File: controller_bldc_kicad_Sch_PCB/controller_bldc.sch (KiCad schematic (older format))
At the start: 57 parts, among them J1 Battery Supply, J2 Emergency Button OUT, J3 Emergency Button IN, J4 Brake, J5 Throttle, J6 LM35, J7 Hall Sensors, J8 Nextion Nx3224T028, J9 BLDC Motor, K1 ADW11, Q1 IRF1010N, Q2 IRF1010N, Q3 IRF1010N, Q4 IRF1010N, Q5 IRF1010N, Q6 IRF1010N, SW1 ON_OFF, SW2 OPC, U1 ESP32-DEVKITC-32D, U2 LM317_TO-220, U3 LM7805_TO220, U4 IR2103, U8 IR2103, U9 IR2103

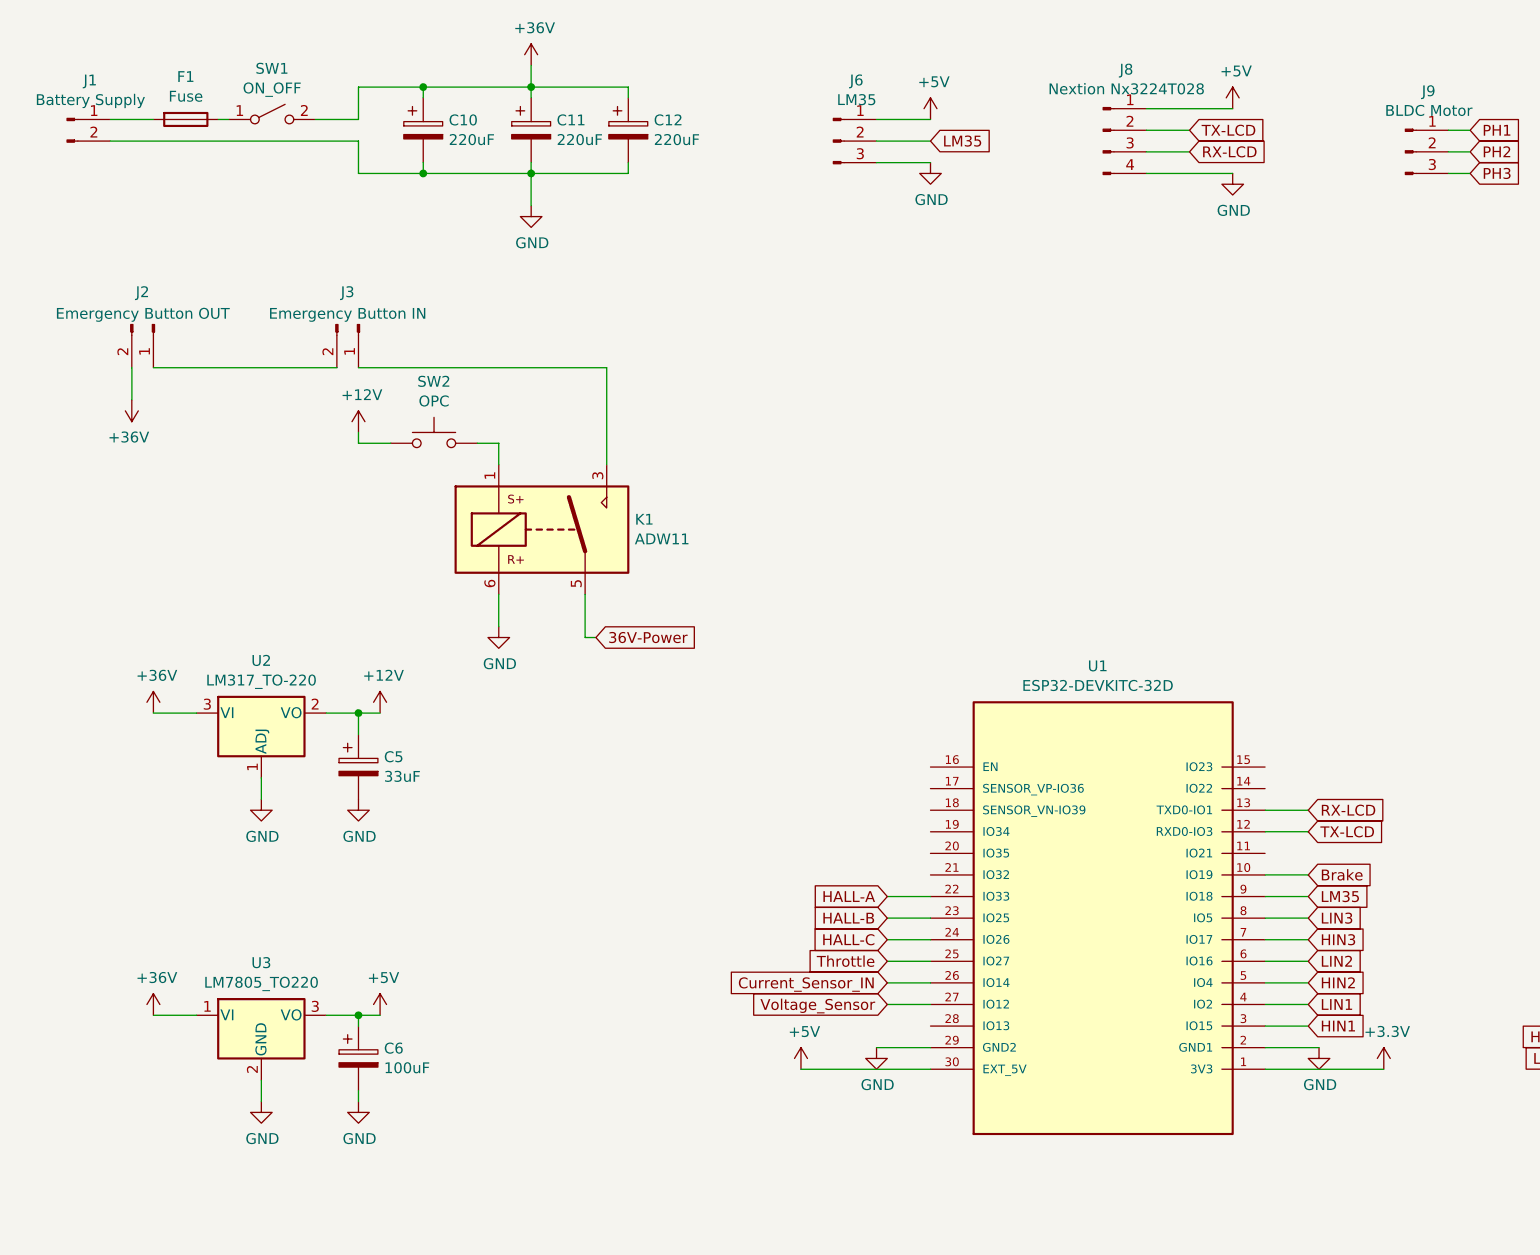
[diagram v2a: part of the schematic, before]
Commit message: Fixed the schematic for the three 220uF capacitors and the connections Connections of MCPWM GPIOs inside the main/*.c were changed to correspond with the schematic
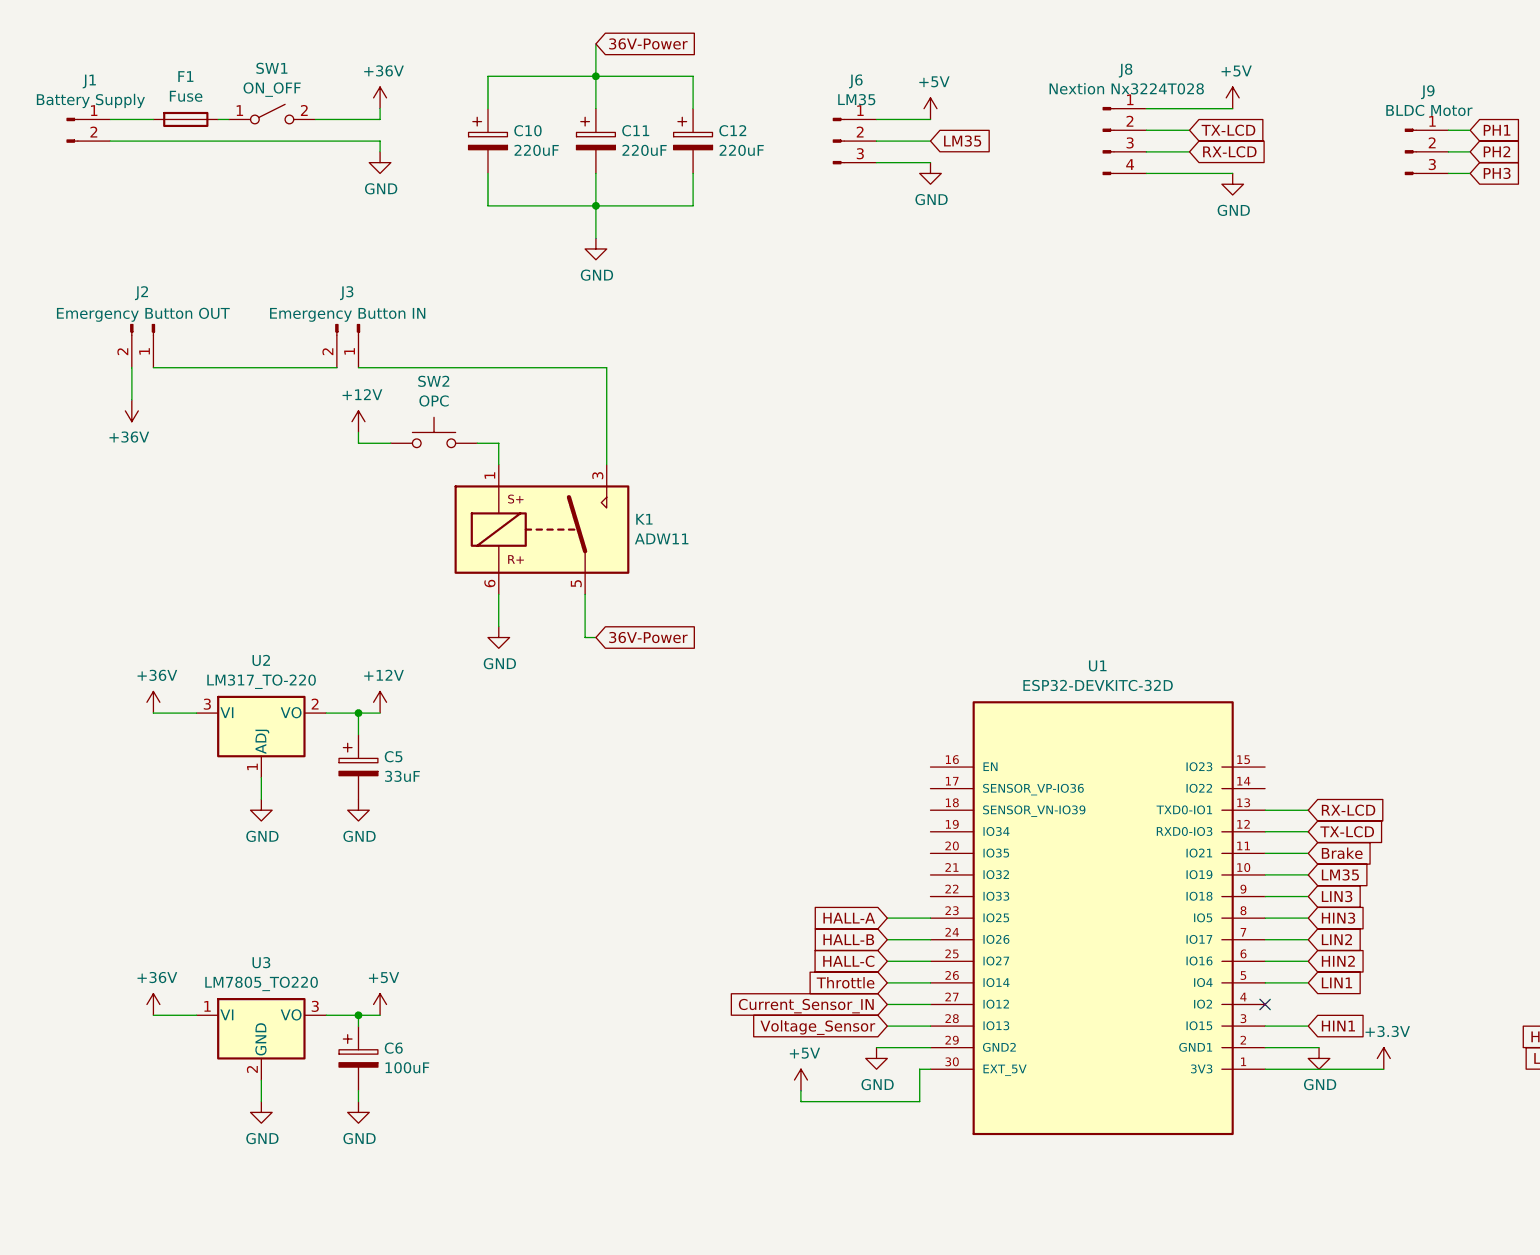
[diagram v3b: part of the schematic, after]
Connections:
- net +36V: no longer C10.1, C11.1, C12.1
- net 36V-Power: now also C10.1, C11.1, C12.1
- net Brake: now also U1.11 (IO21); no longer U1.10 (IO19)
- net Current_Sensor_IN: now also U1.27 (IO12); no longer U1.26 (IO14)
- net HALL-A: now also U1.23 (IO25); no longer U1.22 (IO33)
- net HALL-B: now also U1.24 (IO26); no longer U1.23 (IO25)
- net HALL-C: now also U1.25 (IO27); no longer U1.24 (IO26)
- net HIN2: now also U1.6 (IO16); no longer U1.5 (IO4)
- net HIN3: now also U1.8 (IO5); no longer U1.7 (IO17)
- net LIN1: now also U1.5 (IO4); no longer U1.4 (IO2)
- net LIN2: now also U1.7 (IO17); no longer U1.6 (IO16)
- net LIN3: now also U1.9 (IO18); no longer U1.8 (IO5)
- net LM35: now also U1.10 (IO19); no longer U1.9 (IO18)
- net Throttle: now also U1.26 (IO14); no longer U1.25 (IO27)
- net Voltage_Sensor: now also U1.28 (IO13); no longer U1.27 (IO12)
- no-connect marks 0 -> 1
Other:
- moved on the sheet: C10, C11, C12
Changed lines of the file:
@@
 L power:GND #PWR08
 U 1 1 6069EAE5
-P 2500 900
-F 0 "#PWR08" H 2500 650 50  0001 C CNN
-F 1 "GND" H 2505 727 50  0000 C CNN
-F 2 "" H 2500 900 50  0001 C CNN
-F 3 "" H 2500 900 50  0001 C CNN
-	1    2500 900
+P 1800 650
+F 0 "#PWR08" H 1800 400 50  0001 C CNN
+F 1 "GND" H 1805 477 50  0000 C CNN
+F 2 "" H 1800 650 50  0001 C CNN
+F 3 "" H 1800 650 50  0001 C CNN
+	1    1800 650
 	1    0    0    -1
 $EndComp
@@
 L power:+36V #PWR07
 U 1 1 6069FCB5
-P 2500 250
-F 0 "#PWR07" H 2500 100 50  0001 C CNN
-F 1 "+36V" H 2515 423 50  0000 C CNN
-F 2 "" H 2500 250 50  0001 C CNN
-F 3 "" H 2500 250 50  0001 C CNN
-	1    2500 250
+P 1800 450
+F 0 "#PWR07" H 1800 300 50  0001 C CNN
+F 1 "+36V" H 1815 623 50  0000 C CNN
+F 2 "" H 1800 450 50  0001 C CNN
+F 3 "" H 1800 450 50  0001 C CNN
+	1    1800 450
 	1    0    0    -1
 $EndComp
@@
 Text GLabel 6100 3800 2    50   Input ~ 0
 TX-LCD
-Text GLabel 4150 4100 0    50   Input ~ 0
+Text GLabel 4150 4200 0    50   Input ~ 0
 HALL-A
-Text GLabel 4150 4200 0    50   Input ~ 0
+Text GLabel 4150 4300 0    50   Input ~ 0
 HALL-B
-Text GLabel 4150 4300 0    50   Input ~ 0
+Text GLabel 4150 4400 0    50   Input ~ 0
 HALL-C
-Text GLabel 6100 4600 2    50   Input ~ 0
+Text GLabel 6100 4500 2    50   Input ~ 0
 LIN1
-Text GLabel 6100 4400 2    50   Input ~ 0
+Text GLabel 6100 4300 2    50   Input ~ 0
 LIN2
-Text GLabel 4150 4400 0    50   Input ~ 0
+Text GLabel 4150 4500 0    50   Input ~ 0
 Throttle
-Text GLabel 4150 4500 0    50   Input ~ 0
+Text GLabel 4150 4600 0    50   Input ~ 0
 Current_Sensor_IN
-Text GLabel 4150 4600 0    50   Input ~ 0
+Text GLabel 4150 4700 0    50   Input ~ 0
 Voltage_Sensor
-Text GLabel 6100 4100 2    50   Input ~ 0
+Text GLabel 6100 4000 2    50   Input ~ 0
 LM35
-Text GLabel 6100 4000 2    50   Input ~ 0
+Text GLabel 6100 3900 2    50   Input ~ 0
 Brake
 Text GLabel 8250 2700 2    50   Input ~ 0
@@
 	1700 3250 1800 3250
 Wire Wire Line
-	5900 4600 6100 4600
+	5900 4500 6100 4500
 Wire Wire Line
 	5900 3800 6100 3800
@@
 Wire Wire Line
 	1100 500  1050 500
-Wire Wire Line
-	1500 500  1700 500
-Wire Wire Line
-	550  600  1700 600
 Wire Wire Line
 	1700 1650 2850 1650
@@
 L Device:CP C10
 U 1 1 60B587DD
-P 2000 550
-F 0 "C10" H 2118 596 50  0000 L CNN
-F 1 "220uF" H 2118 505 50  0000 L CNN
-F 2 "Capacitor_SMD:CP_Elec_10x14.3" H 2118 459 50  0001 L CNN
-F 3 "~" H 2000 550 50  0001 C CNN
-	1    2000 550
-	1    0    0    -1
-$EndComp
-Wire Wire Line
-	2000 700  2000 750
-Wire Wire Line
-	2000 750  1700 750
-Wire Wire Line
-	1700 750  1700 600
-Connection ~ 2000 750
-Wire Wire Line
-	2000 400  2000 350
-Wire Wire Line
-	2000 350  1700 350
-Wire Wire Line
-	1700 350  1700 500
-Connection ~ 2000 350
-Wire Wire Line
-	5900 4200 6100 4200
-Text GLabel 6100 4200 2    50   Input ~ 0
+P 2300 600
+F 0 "C10" H 2418 646 50  0000 L CNN
+F 1 "220uF" H 2418 555 50  0000 L CNN
+F 2 "Capacitor_SMD:CP_Elec_10x14.3" H 2418 509 50  0001 L CNN
+F 3 "~" H 2300 600 50  0001 C CNN
+	1    2300 600
+	1    0    0    -1
+$EndComp
+Wire Wire Line
+	5900 4100 6100 4100
+Text GLabel 6100 4100 2    50   Input ~ 0
 LIN3
-Text GLabel 6100 4500 2    50   Input ~ 0
+Text GLabel 6100 4400 2    50   Input ~ 0
 HIN2
 Wire Wire Line
-	5900 4500 6100 4500
+	5900 4400 6100 4400
 Text GLabel 6100 4700 2    50   Input ~ 0
 HIN1
@@
 	6100 4700 5900 4700
 Wire Wire Line
-	6100 4400 5900 4400
-Text GLabel 6100 4300 2    50   Input ~ 0
+	6100 4300 5900 4300
+Text GLabel 6100 4200 2    50   Input ~ 0
 HIN3
 Wire Wire Line
-	6100 4300 5900 4300
-Wire Wire Line
-	6100 4100 5900 4100
+	6100 4200 5900 4200
 Wire Wire Line
 	6100 4000 5900 4000
+Wire Wire Line
+	6100 3900 5900 3900
 Wire Wire Line
 	6150 4800 5900 4800
@@
 L power:+5V #PWR0102
 U 1 1 60D5293D
-P 3750 4900
-F 0 "#PWR0102" H 3750 4750 50  0001 C CNN
-F 1 "+5V" H 3765 5073 50  0000 C CNN
-F 2 "" H 3750 4900 50  0001 C CNN
-F 3 "" H 3750 4900 50  0001 C CNN
-	1    3750 4900
+P 3750 5000
+F 0 "#PWR0102" H 3750 4850 50  0001 C CNN
+F 1 "+5V" H 3765 5173 50  0000 C CNN
+F 2 "" H 3750 5000 50  0001 C CNN
+F 3 "" H 3750 5000 50  0001 C CNN
+	1    3750 5000
 	1    0    0    -1
 $EndComp
@@
 L Device:CP C11
 U 1 1 60DBB821
-P 2500 550
-F 0 "C11" H 2618 596 50  0000 L CNN
-F 1 "220uF" H 2618 505 50  0000 L CNN
-F 2 "Capacitor_SMD:CP_Elec_10x14.3" H 2538 400 50  0001 C CNN
-F 3 "~" H 2500 550 50  0001 C CNN
-	1    2500 550
+P 2800 600
+F 0 "C11" H 2918 646 50  0000 L CNN
+F 1 "220uF" H 2918 555 50  0000 L CNN
+F 2 "Capacitor_SMD:CP_Elec_10x14.3" H 2838 450 50  0001 C CNN
+F 3 "~" H 2800 600 50  0001 C CNN
+	1    2800 600
 	1    0    0    -1
 $EndComp
@@
 L Device:CP C12
 U 1 1 60DBBBDB
-P 2950 550
-F 0 "C12" H 3068 596 50  0000 L CNN
-F 1 "220uF" H 3068 505 50  0000 L CNN
-F 2 "Capacitor_SMD:CP_Elec_10x14.3" H 2988 400 50  0001 C CNN
-F 3 "~" H 2950 550 50  0001 C CNN
-	1    2950 550
-	1    0    0    -1
-$EndComp
-Wire Wire Line
-	2000 350  2500 350
-Wire Wire Line
-	2500 350  2500 400
-Wire Wire Line
-	2500 350  2950 350
-Wire Wire Line
-	2950 350  2950 400
-Connection ~ 2500 350
-Wire Wire Line
-	2500 700  2500 750
-Wire Wire Line
-	2500 750  2000 750
-Wire Wire Line
-	2950 700  2950 750
-Wire Wire Line
-	2950 750  2500 750
-Connection ~ 2500 750
-Wire Wire Line
-	2500 250  2500 350
-Wire Wire Line
-	2500 900  2500 750
+P 3250 600
+F 0 "C12" H 3368 646 50  0000 L CNN
+F 1 "220uF" H 3368 555 50  0000 L CNN
+F 2 "Capacitor_SMD:CP_Elec_10x14.3" H 3288 450 50  0001 C CNN
+F 3 "~" H 3250 600 50  0001 C CNN
+	1    3250 600
+	1    0    0    -1
+$EndComp
 $Comp
 L power:+12V #PWR0110
@@
 Connection ~ 7850 1800
 Wire Wire Line
+	4150 4400 4350 4400
+Wire Wire Line
 	4150 4300 4350 4300
 Wire Wire Line
 	4150 4200 4350 4200
 Wire Wire Line
-	4150 4100 4350 4100
-Wire Wire Line
 	4350 4800 4100 4800
 Wire Wire Line
-	3750 4900 4350 4900
-Wire Wire Line
-	4150 4600 4350 4600
-Wire Wire Line
-	4350 4500 4150 4500
-Wire Wire Line
-	4150 4400 4350 4400
+	4150 4700 4350 4700
+Wire Wire Line
+	4350 4600 4150 4600
+Wire Wire Line
+	4150 4500 4350 4500
 $Comp
 L ESP32-DEVKITC-32D:ESP32-DEVKITC-32D U1
@@
 	1    0    0    -1
 $EndComp
+Wire Wire Line
+	3750 5050 4300 5050
+Wire Wire Line
+	4300 5050 4300 4900
+Wire Wire Line
+	4300 4900 4350 4900
+Wire Wire Line
+	3750 5000 3750 5050
+NoConn ~ 5900 4600
+Wire Wire Line
+	1500 500  1800 500
+Wire Wire Line
+	1800 500  1800 450
+Wire Wire Line
+	1800 650  1800 600
+Wire Wire Line
+	1800 600  550  600
+Wire Wire Line
+	2300 450  2300 300
+Wire Wire Line
+	2300 300  2800 300
+Wire Wire Line
+	2800 300  2800 450
+Wire Wire Line
+	3250 450  3250 300
+Wire Wire Line
+	3250 300  2800 300
+Connection ~ 2800 300
+Wire Wire Line
+	2300 750  2300 900
+Wire Wire Line
+	2300 900  2800 900
+Wire Wire Line
+	2800 900  2800 750
+Wire Wire Line
+	3250 750  3250 900
+Wire Wire Line
+	3250 900  2800 900
+Connection ~ 2800 900
+$Comp
+L power:GND #PWR?
+U 1 1 608A0585
+P 2800 1050
+F 0 "#PWR?" H 2800 800 50  0001 C CNN
+F 1 "GND" H 2805 877 50  0000 C CNN
+F 2 "" H 2800 1050 50  0001 C CNN
+F 3 "" H 2800 1050 50  0001 C CNN
+	1    2800 1050
+	1    0    0    -1
+$EndComp
+Wire Wire Line
+	2800 1050 2800 900
+Text GLabel 2800 150  2    50   Input ~ 0
+36V-Power
+Wire Wire Line
+	2800 150  2800 300
 $EndSCHEMATC

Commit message: PCB: Added Amp Op library and changed V & A Sensors
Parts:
- R16, R4: value 2.2k -> 10k
- U1: symbol ESP32-DEVKITC-32D:ESP32-DEVKITC-32D -> controller_bldc-rescue:ESP32-DEVKITC-32D-ESP32-DEVKITC-32D
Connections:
- net Current_Sensor_IN: now also C13.2, R16.1; no longer C13.1
- net GND: now also C1.1, C13.1
- net Voltage_Sensor: now also C1.2, R4.1; no longer C1.1
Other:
- moved on the sheet: C1, C13
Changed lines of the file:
@@
 P 3200 6900
 F 0 "R4" V 2993 6900 50  0000 C CNN
-F 1 "2.2k" V 3084 6900 50  0000 C CNN
+F 1 "10k" V 3084 6900 50  0000 C CNN
 F 2 "Resistor_THT:R_Axial_DIN0207_L6.3mm_D2.5mm_P10.16mm_Horizontal" V 3130 6900 50  0001 C CNN
 F 3 "~" H 3200 6900 50  0001 C CNN
@@
 L Device:C_Small C1
 U 1 1 6082364C
-P 3500 6900
-F 0 "C1" V 3271 6900 50  0000 C CNN
-F 1 "0.1uF" V 3362 6900 50  0000 C CNN
-F 2 "Capacitor_THT:C_Disc_D7.5mm_W5.0mm_P10.00mm" H 3500 6900 50  0001 C CNN
-F 3 "~" H 3500 6900 50  0001 C CNN
-	1    3500 6900
-	0    1    1    0
+P 3500 7200
+F 0 "C1" H 3350 7100 50  0000 C CNN
+F 1 "0.1uF" H 3300 7250 50  0000 C CNN
+F 2 "Capacitor_THT:C_Disc_D7.5mm_W5.0mm_P10.00mm" H 3500 7200 50  0001 C CNN
+F 3 "~" H 3500 7200 50  0001 C CNN
+	1    3500 7200
+	-1   0    0    1
 $EndComp
 Wire Wire Line
@@
 Wire Wire Line
 	2850 6900 2850 6950
-Wire Wire Line
-	3350 6900 3400 6900
-Wire Wire Line
-	3650 6900 3600 6900
 $Comp
 L Device:R R2
@@
 	4150 4500 4350 4500
 $Comp
-L ESP32-DEVKITC-32D:ESP32-DEVKITC-32D U1
+L controller_bldc-rescue:ESP32-DEVKITC-32D-ESP32-DEVKITC-32D U1
 U 1 1 6081E288
 P 5150 4200
@@
 P 5400 6700
 F 0 "R16" V 5193 6700 50  0000 C CNN
-F 1 "2.2k" V 5284 6700 50  0000 C CNN
+F 1 "10k" V 5284 6700 50  0000 C CNN
 F 2 "Resistor_THT:R_Axial_DIN0207_L6.3mm_D2.5mm_P10.16mm_Horizontal" V 5330 6700 50  0001 C CNN
 F 3 "~" H 5400 6700 50  0001 C CNN
@@
 L Device:C_Small C13
 U 1 1 60885D9B
-P 5900 6700
-F 0 "C13" V 5671 6700 50  0000 C CNN
-F 1 "0.1uF" V 5762 6700 50  0000 C CNN
-F 2 "Capacitor_THT:C_Disc_D7.5mm_W5.0mm_P10.00mm" H 5900 6700 50  0001 C CNN
-F 3 "~" H 5900 6700 50  0001 C CNN
-	1    5900 6700
-	0    1    1    0
+P 5950 7000
+F 0 "C13" V 5721 7000 50  0000 C CNN
+F 1 "0.1uF" V 5812 7000 50  0000 C CNN
+F 2 "Capacitor_THT:C_Disc_D7.5mm_W5.0mm_P10.00mm" H 5950 7000 50  0001 C CNN
+F 3 "~" H 5950 7000 50  0001 C CNN
+	1    5950 7000
+	-1   0    0    1
 $EndComp
 Wire Wire Line
@@
 Wire Wire Line
 	4950 6700 5250 6700
-Wire Wire Line
-	5550 6700 5800 6700
 Text GLabel 6250 6700 2    50   Input ~ 0
 Current_Sensor_IN
-Wire Wire Line
-	6000 6700 6250 6700
 $Comp
 L power:+12V #PWR0115
@@
 Wire Wire Line
 	2800 150  2800 300
+$Comp
+L power:GND #PWR?
+U 1 1 6084D0EA
+P 5950 7200
+F 0 "#PWR?" H 5950 6950 50  0001 C CNN
+F 1 "GND" H 5955 7027 50  0000 C CNN
+F 2 "" H 5950 7200 50  0001 C CNN
+F 3 "" H 5950 7200 50  0001 C CNN
+	1    5950 7200
+	1    0    0    -1
+$EndComp
+Wire Wire Line
+	5950 7100 5950 7200
+Wire Wire Line
+	5950 6900 5950 6700
+Wire Wire Line
+	5550 6700 5950 6700
+Wire Wire Line
+	5950 6700 6250 6700
+Connection ~ 5950 6700
+Wire Wire Line
+	3500 6900 3500 7100
+Wire Wire Line
+	3350 6900 3500 6900
+Wire Wire Line
+	3500 6900 3650 6900
+Connection ~ 3500 6900
+$Comp
+L power:GND #PWR?
+U 1 1 60892AC0
+P 3500 7350
+F 0 "#PWR?" H 3500 7100 50  0001 C CNN
+F 1 "GND" H 3505 7177 50  0000 C CNN
+F 2 "" H 3500 7350 50  0001 C CNN
+F 3 "" H 3500 7350 50  0001 C CNN
+	1    3500 7350
+	1    0    0    -1
+$EndComp
+Wire Wire Line
+	3500 7300 3500 7350
 $EndSCHEMATC
